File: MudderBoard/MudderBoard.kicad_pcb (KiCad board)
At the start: 2 copper layers, 248.2 x 122.9 mm, 157 parts, among them K1 AZ2850-2A-12DE, M1 NMOS, M2 NMOS, M3 N-MOSFET, M4 N-MOSFET, Q1 CSD16327Q3, Q2 NPN, U1 LM5122QMH/NOPB, U2 TPS566242DRLR, U3 LP38691DTX-3.3/NOPB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

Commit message: Schematic updates
global labels and test points
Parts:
- added TP36: TestPoint, TestPoint:TestPoint_Pad_1.0x1.0mm, F.Cu at (183.0, 79.5)
- added TP37: TestPoint, TestPoint:TestPoint_Pad_1.5x1.5mm, F.Cu at (191.0, 57.8)
- added TP38: TestPoint, TestPoint:TestPoint_Pad_D1.0mm, F.Cu at (181.5, 45.0)
- moved C23 138.6 mm to (-59.6, 146.0)
- moved C24 138.6 mm to (-59.6, 148.5)
- moved C29 138.6 mm to (-72.8, 153.9)
- moved C30 138.6 mm to (-77.3, 154.0)
- moved C31 138.6 mm to (-72.8, 156.9)
- moved C32 138.6 mm to (-77.3, 157.1)
- moved D5 138.6 mm to (-56.6, 152.0)
- moved D6 138.6 mm to (-56.6, 156.5)
- moved D7 138.6 mm to (-58.6, 138.4)
- moved D8 138.6 mm to (-58.6, 142.7)
- moved L4 138.6 mm to (-65.9, 139.7)
- moved L5 138.6 mm to (-65.9, 146.4)
- moved R30 138.6 mm to (-65.6, 152.3)
- moved R31 138.6 mm to (-65.6, 157.3)
- moved R34 138.6 mm to (-56.2, 145.9)
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
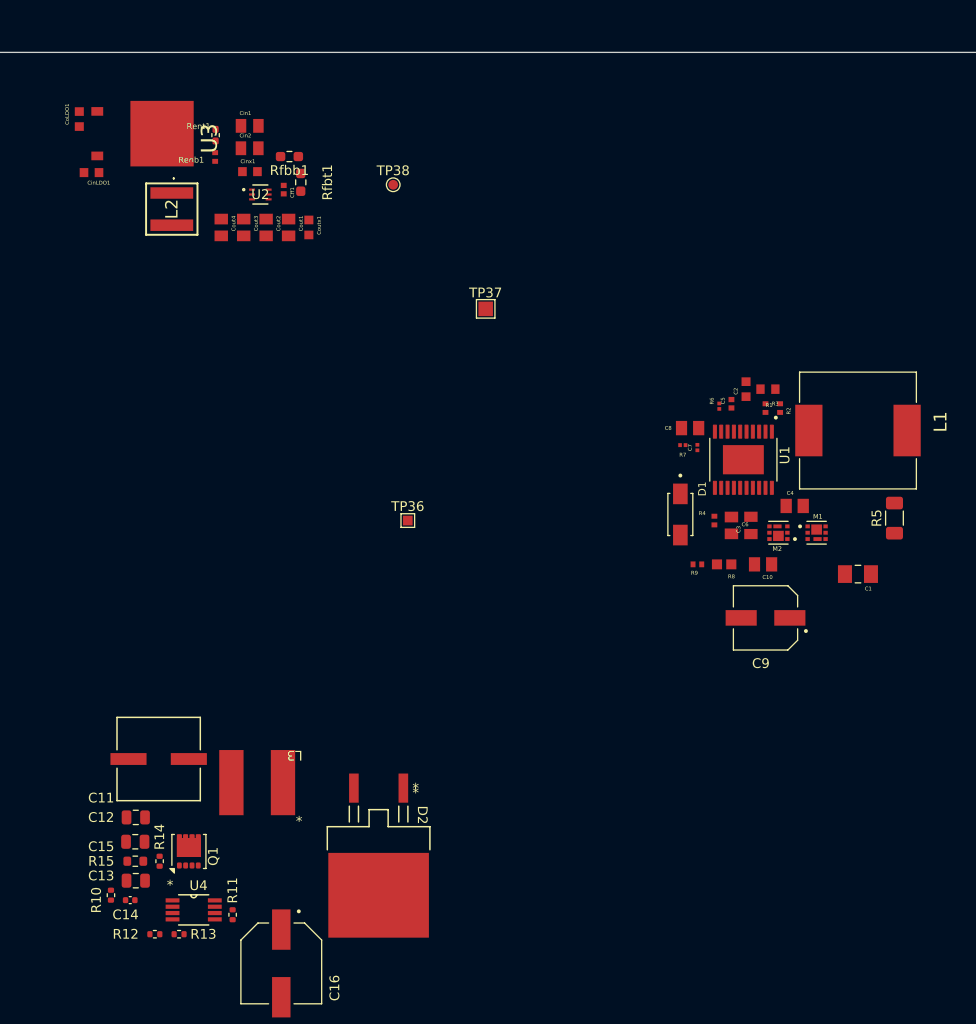
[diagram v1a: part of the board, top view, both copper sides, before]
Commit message: Schematic and Layout
TPs and net labels
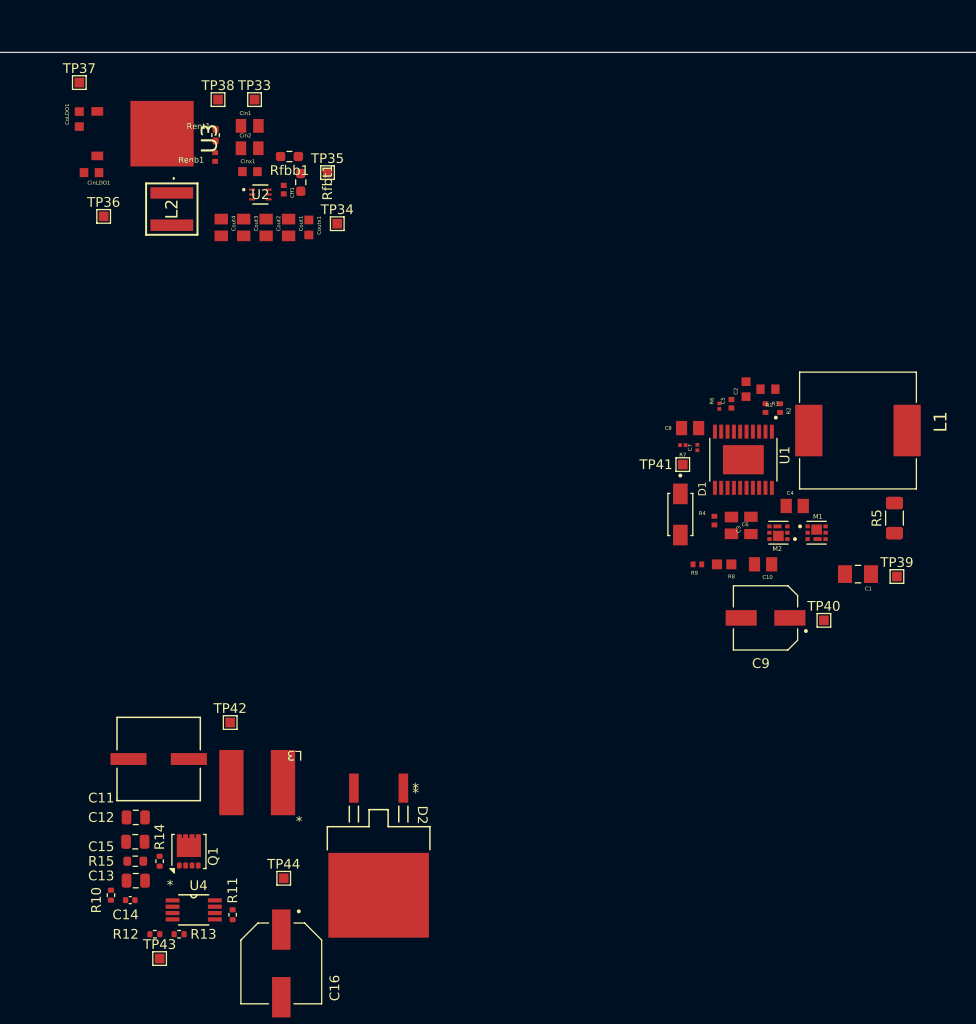
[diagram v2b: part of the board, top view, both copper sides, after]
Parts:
- added TP33: TestPoint, TestPoint:TestPoint_Pad_1.0x1.0mm, F.Cu at (167.2, 36.2)
- added TP34: TestPoint, TestPoint:TestPoint_Pad_1.0x1.0mm, F.Cu at (175.8, 49.0)
- added TP35: TestPoint, TestPoint:TestPoint_Pad_1.0x1.0mm, F.Cu at (174.8, 43.8)
- added TP39: TestPoint, TestPoint:TestPoint_Pad_1.0x1.0mm, F.Cu at (233.2, 85.2)
- added TP40: TestPoint, TestPoint:TestPoint_Pad_1.0x1.0mm, F.Cu at (225.8, 89.8)
- added TP41: TestPoint, TestPoint:TestPoint_Pad_1.0x1.0mm, F.Cu at (211.2, 73.8)
- added TP42: TestPoint, TestPoint:TestPoint_Pad_1.0x1.0mm, F.Cu at (164.8, 100.2)
- added TP43: TestPoint, TestPoint:TestPoint_Pad_1.0x1.0mm, F.Cu at (157.5, 124.5)
- added TP44: TestPoint, TestPoint:TestPoint_Pad_1.0x1.0mm, F.Cu at (170.2, 116.2)
- TP37: footprint TestPoint:TestPoint_Pad_1.5x1.5mm -> TestPoint:TestPoint_Pad_1.0x1.0mm
- TP38: footprint TestPoint:TestPoint_Pad_D1.0mm -> TestPoint:TestPoint_Pad_1.0x1.0mm
- moved TP37 47.8 mm to (149.2, 34.5)
- moved TP36 44.2 mm to (151.8, 48.2)
- moved TP38 20.0 mm to (163.5, 36.2)
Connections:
- net /LiDar/+24V renamed +24V
- net Net-(C16-Pad1) renamed +19V
- C1 pad 1: /LiDar/+BATT -> +BATT
- R1 pad 1: /LiDar/+BATT -> +BATT
- R3 pad 1: /LiDar/+BATT -> +BATT
- R5 pad 1: /LiDar/+BATT -> +BATT
- U1 pad 4: /LiDar/+BATT -> +BATT

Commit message: Update
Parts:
- moved TP10 12.3 mm to (-47.7, 112.2)
- moved TP11 12.3 mm to (-47.7, 116.6)
- moved TP12 12.3 mm to (-47.7, 121.0)
- moved TP13 12.3 mm to (-47.7, 125.3)
- moved TP14 12.3 mm to (-47.7, 129.7)
- moved TP15 12.3 mm to (-43.4, 103.5)
- moved TP16 12.3 mm to (-43.4, 107.9)
- moved TP17 12.3 mm to (-43.4, 112.2)
- moved TP18 12.3 mm to (-43.4, 116.6)
- moved TP19 12.3 mm to (-43.4, 121.0)
- moved TP20 12.3 mm to (-43.4, 125.3)
- moved TP21 12.3 mm to (-43.4, 129.7)
- moved TP29 12.3 mm to (-33.0, 104.2)
- moved TP30 12.3 mm to (-33.0, 108.5)
- moved TP31 12.3 mm to (-33.0, 112.8)
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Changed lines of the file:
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@@
 	(footprint "TestPoint:TestPoint_Keystone_5000-5004_Miniature"
 		(layer "F.Cu")
-		(at -31.15 105.05)
+		(at -43.35 103.55)
 		(descr "Keystone Miniature THM Test Point 5000-5004, http://www.keyelco.com/product-pdf.cfm?p=1309")
 		(tags "Through Hole Mount Test Points")
@@
 	(footprint "TestPoint:TestPoint_Keystone_5000-5004_Miniature"
 		(layer "F.Cu")
-		(at -26.8 122.45)
+		(at -39 120.95)
 		(descr "Keystone Miniature THM Test Point 5000-5004, http://www.keyelco.com/product-pdf.cfm?p=1309")
 		(tags "Through Hole Mount Test Points")
@@
 	(footprint "TestPoint:TestPoint_Keystone_5000-5004_Miniature"
 		(layer "F.Cu")
-		(at -39.85 131.15)
+		(at -52.05 129.65)
 		(descr "Keystone Miniature THM Test Point 5000-5004, http://www.keyelco.com/product-pdf.cfm?p=1309")
 		(tags "Through Hole Mount Test Points")
@@
 	(footprint "TestPoint:TestPoint_Keystone_5000-5004_Miniature"
 		(layer "F.Cu")
-		(at -35.5 105.05)
+		(at -47.7 103.55)
 		(descr "Keystone Miniature THM Test Point 5000-5004, http://www.keyelco.com/product-pdf.cfm?p=1309")
 		(tags "Through Hole Mount Test Points")
@@
 	(footprint "TestPoint:TestPoint_Keystone_5000-5004_Miniature"
 		(layer "F.Cu")
-		(at -31.15 122.45)
+		(at -43.35 120.95)
 		(descr "Keystone Miniature THM Test Point 5000-5004, http://www.keyelco.com/product-pdf.cfm?p=1309")
 		(tags "Through Hole Mount Test Points")
@@
 	(footprint "TestPoint:TestPoint_Keystone_5000-5004_Miniature"
 		(layer "F.Cu")
-		(at -20.75 114.35)
+		(at -32.95 112.85)
 		(descr "Keystone Miniature THM Test Point 5000-5004, http://www.keyelco.com/product-pdf.cfm?p=1309")
 		(tags "Through Hole Mount Test Points")
@@
 	(footprint "TestPoint:TestPoint_Keystone_5000-5004_Miniature"
 		(layer "F.Cu")
-		(at -39.85 118.1)
+		(at -52.05 116.6)
 		(descr "Keystone Miniature THM Test Point 5000-5004, http://www.keyelco.com/product-pdf.cfm?p=1309")
 		(tags "Through Hole Mount Test Points")
@@
 	(footprint "TestPoint:TestPoint_Keystone_5000-5004_Miniature"
 		(layer "F.Cu")
-		(at -35.5 122.45)
+		(at -47.7 120.95)
 		(descr "Keystone Miniature THM Test Point 5000-5004, http://www.keyelco.com/product-pdf.cfm?p=1309")
 		(tags "Through Hole Mount Test Points")
@@
 	(footprint "TestPoint:TestPoint_Keystone_5000-5004_Miniature"
 		(layer "F.Cu")
-		(at -26.8 131.15)
+		(at -39 129.65)
 		(descr "Keystone Miniature THM Test Point 5000-5004, http://www.keyelco.com/product-pdf.cfm?p=1309")
 		(tags "Through Hole Mount Test Points")
@@
 	(footprint "TestPoint:TestPoint_Keystone_5000-5004_Miniature"
 		(layer "F.Cu")
-		(at -39.85 109.4)
+		(at -52.05 107.9)
 		(descr "Keystone Miniature THM Test Point 5000-5004, http://www.keyelco.com/product-pdf.cfm?p=1309")
 		(tags "Through Hole Mount Test Points")
@@
 	(footprint "TestPoint:TestPoint_Keystone_5000-5004_Miniature"
 		(layer "F.Cu")
-		(at -39.85 113.75)
+		(at -52.05 112.25)
 		(descr "Keystone Miniature THM Test Point 5000-5004, http://www.keyelco.com/product-pdf.cfm?p=1309")
 		(tags "Through Hole Mount Test Points")
@@
 	(footprint "TestPoint:TestPoint_Keystone_5000-5004_Miniature"
 		(layer "F.Cu")
-		(at -35.5 109.4)
+		(at -47.7 107.9)
 		(descr "Keystone Miniature THM Test Point 5000-5004, http://www.keyelco.com/product-pdf.cfm?p=1309")
 		(tags "Through Hole Mount Test Points")
@@
 	(footprint "TestPoint:TestPoint_Keystone_5000-5004_Miniature"
 		(layer "F.Cu")
-		(at -35.5 126.8)
+		(at -47.7 125.3)
 		(descr "Keystone Miniature THM Test Point 5000-5004, http://www.keyelco.com/product-pdf.cfm?p=1309")
 		(tags "Through Hole Mount Test Points")
@@
 	(footprint "TestPoint:TestPoint_Keystone_5000-5004_Miniature"
 		(layer "F.Cu")
-		(at -31.15 118.1)
+		(at -43.35 116.6)
 		(descr "Keystone Miniature THM Test Point 5000-5004, http://www.keyelco.com/product-pdf.cfm?p=1309")
 		(tags "Through Hole Mount Test Points")
@@
 	(footprint "TestPoint:TestPoint_Keystone_5000-5004_Miniature"
 		(layer "F.Cu")
-		(at -35.5 118.1)
+		(at -47.7 116.6)
 		(descr "Keystone Miniature THM Test Point 5000-5004, http://www.keyelco.com/product-pdf.cfm?p=1309")
 		(tags "Through Hole Mount Test Points")
@@
 	(footprint "TestPoint:TestPoint_Keystone_5000-5004_Miniature"
 		(layer "F.Cu")
-		(at -26.8 113.75)
+		(at -39 112.25)
 		(descr "Keystone Miniature THM Test Point 5000-5004, http://www.keyelco.com/product-pdf.cfm?p=1309")
 		(tags "Through Hole Mount Test Points")
@@
 	(footprint "TestPoint:TestPoint_Keystone_5000-5004_Miniature"
 		(layer "F.Cu")
-		(at -26.8 118.1)
+		(at -39 116.6)
 		(descr "Keystone Miniature THM Test Point 5000-5004, http://www.keyelco.com/product-pdf.cfm?p=1309")
 		(tags "Through Hole Mount Test Points")
@@
 	(footprint "TestPoint:TestPoint_Keystone_5000-5004_Miniature"
 		(layer "F.Cu")
-		(at -31.15 113.75)
+		(at -43.35 112.25)
 		(descr "Keystone Miniature THM Test Point 5000-5004, http://www.keyelco.com/product-pdf.cfm?p=1309")
 		(tags "Through Hole Mount Test Points")
@@
 	(footprint "TestPoint:TestPoint_Keystone_5000-5004_Miniature"
 		(layer "F.Cu")
-		(at -31.15 126.8)
+		(at -43.35 125.3)
 		(descr "Keystone Miniature THM Test Point 5000-5004, http://www.keyelco.com/product-pdf.cfm?p=1309")
 		(tags "Through Hole Mount Test Points")
@@
 	(footprint "TestPoint:TestPoint_Keystone_5000-5004_Miniature"
 		(layer "F.Cu")
-		(at -20.75 105.65)
+		(at -32.95 104.15)
 		(descr "Keystone Miniature THM Test Point 5000-5004, http://www.keyelco.com/product-pdf.cfm?p=1309")
 		(tags "Through Hole Mount Test Points")
@@
 	(footprint "TestPoint:TestPoint_Keystone_5000-5004_Miniature"
 		(layer "F.Cu")
-		(at -20.75 110)
+		(at -32.95 108.5)
 		(descr "Keystone Miniature THM Test Point 5000-5004, http://www.keyelco.com/product-pdf.cfm?p=1309")
 		(tags "Through Hole Mount Test Points")
@@
 	(footprint "TestPoint:TestPoint_Keystone_5000-5004_Miniature"
 		(layer "F.Cu")
-		(at -39.85 122.45)
+		(at -52.05 120.95)
 		(descr "Keystone Miniature THM Test Point 5000-5004, http://www.keyelco.com/product-pdf.cfm?p=1309")
 		(tags "Through Hole Mount Test Points")
@@
 	(footprint "TestPoint:TestPoint_Keystone_5000-5004_Miniature"
 		(layer "F.Cu")
-		(at -31.15 109.4)
+		(at -43.35 107.9)
 		(descr "Keystone Miniature THM Test Point 5000-5004, http://www.keyelco.com/product-pdf.cfm?p=1309")
 		(tags "Through Hole Mount Test Points")
@@
 	(footprint "TestPoint:TestPoint_Keystone_5000-5004_Miniature"
 		(layer "F.Cu")
-		(at -26.8 105.05)
+		(at -39 103.55)
 		(descr "Keystone Miniature THM Test Point 5000-5004, http://www.keyelco.com/product-pdf.cfm?p=1309")
 		(tags "Through Hole Mount Test Points")
@@
 	(footprint "TestPoint:TestPoint_Keystone_5000-5004_Miniature"
 		(layer "F.Cu")
-		(at -20.75 118.7)
+		(at -32.95 117.2)
 		(descr "Keystone Miniature THM Test Point 5000-5004, http://www.keyelco.com/product-pdf.cfm?p=1309")
 		(tags "Through Hole Mount Test Points")
@@
 	(footprint "TestPoint:TestPoint_Keystone_5000-5004_Miniature"
 		(layer "F.Cu")
-		(at -35.5 113.75)
+		(at -47.7 112.25)
 		(descr "Keystone Miniature THM Test Point 5000-5004, http://www.keyelco.com/product-pdf.cfm?p=1309")
 		(tags "Through Hole Mount Test Points")
@@
 	(footprint "TestPoint:TestPoint_Keystone_5000-5004_Miniature"
 		(layer "F.Cu")
-		(at -26.8 126.8)
+		(at -39 125.3)
 		(descr "Keystone Miniature THM Test Point 5000-5004, http://www.keyelco.com/product-pdf.cfm?p=1309")
 		(tags "Through Hole Mount Test Points")
@@
 	(footprint "TestPoint:TestPoint_Keystone_5000-5004_Miniature"
 		(layer "F.Cu")
-		(at -26.8 109.4)
+		(at -39 107.9)
 		(descr "Keystone Miniature THM Test Point 5000-5004, http://www.keyelco.com/product-pdf.cfm?p=1309")
 		(tags "Through Hole Mount Test Points")
@@
 	(footprint "TestPoint:TestPoint_Keystone_5000-5004_Miniature"
 		(layer "F.Cu")
-		(at -39.85 126.8)
+		(at -52.05 125.3)
 		(descr "Keystone Miniature THM Test Point 5000-5004, http://www.keyelco.com/product-pdf.cfm?p=1309")
 		(tags "Through Hole Mount Test Points")
@@
 	(footprint "TestPoint:TestPoint_Keystone_5000-5004_Miniature"
 		(layer "F.Cu")
-		(at -35.5 131.15)
+		(at -47.7 129.65)
 		(descr "Keystone Miniature THM Test Point 5000-5004, http://www.keyelco.com/product-pdf.cfm?p=1309")
 		(tags "Through Hole Mount Test Points")
@@
 	(footprint "TestPoint:TestPoint_Keystone_5000-5004_Miniature"
 		(layer "F.Cu")
-		(at -31.15 131.15)
+		(at -43.35 129.65)
 		(descr "Keystone Miniature THM Test Point 5000-5004, http://www.keyelco.com/product-pdf.cfm?p=1309")
 		(tags "Through Hole Mount Test Points")
@@
 	(footprint "TestPoint:TestPoint_Keystone_5000-5004_Miniature"
 		(layer "F.Cu")
-		(at -39.85 105.05)
+		(at -52.05 103.55)
 		(descr "Keystone Miniature THM Test Point 5000-5004, http://www.keyelco.com/product-pdf.cfm?p=1309")
 		(tags "Through Hole Mount Test Points")

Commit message: Layout
ESC
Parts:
- removed L4, L5: 2.352uH, Inductor_SMD:L_Neosid_SM-PIC0512H
- removed M3, M4: N-MOSFET, Lidar_Foot:TRANS_CSD17308Q3
- added Q3: CSD16340Q3, ColinFET1:TRANS_CSD16340Q3, F.Cu at (69.2, 123.2)
- added Q4: CSD16340Q3, ColinFET1:TRANS_CSD16340Q3, F.Cu at (127.4, 125.2)
- added Q5: CSD16340Q3, ColinFET1:TRANS_CSD16340Q3, F.Cu at (132.2, 125.2)
- added Q7: CSD16340Q3, ColinFET1:TRANS_CSD16340Q3, F.Cu at (74.0, 123.2)
- added TP28: TestPoint, TestPoint:TestPoint_Keystone_5000-5004_Miniature, F.Cu at (-99.8, 143.9)
- moved R31 210.3 mm to (142.0, 124.2), turned to -90 degrees
- moved C32 210.1 mm to (129.4, 119.2)
- moved U9 200.1 mm to (123.0, 116.2), turned to -90 degrees
- moved C31 195.2 mm to (118.0, 115.8), turned to 90 degrees
- moved C24 187.1 mm to (123.0, 107.8), turned to 90 degrees
- moved D8 176.8 mm to (117.8, 130.8), turned to -90 degrees
- moved D6 175.7 mm to (115.5, 121.0), turned to -90 degrees
- moved C22 174.2 mm to (141.5, 138.5), turned to 180 degrees
- moved R35 173.7 mm to (116.2, 127.0)
- moved C38 172.5 mm to (125.2, 138.0)
- moved R26 171.5 mm to (126.8, 109.8), turned to -90 degrees
- moved C36 171.0 mm to (124.0, 122.0), turned to -90 degrees
- moved C34 167.6 mm to (121.8, 122.0), turned to -90 degrees
- moved R27 167.5 mm to (127.2, 108.0), turned to 180 degrees
- moved C26 166.1 mm to (123.0, 111.0), turned to 90 degrees
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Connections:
- TP29 pad 1: unconnected-(TP29-Pad1) -> HO
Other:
- board size 248.2 x 122.9 mm -> 248.2 x 129.9 mm
- board text added: "INDUCTOR"
